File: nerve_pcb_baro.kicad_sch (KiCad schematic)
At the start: 5 parts

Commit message: Update schematics
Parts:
- JP2: footprint (none) -> Jumper:SolderJumper-2_P1.3mm_Open_TrianglePad1.0x1.5mm
- R22: renamed from R21; footprint (none) -> Resistor_SMD:R_0402_1005Metric
- R23: renamed from R22; footprint (none) -> Resistor_SMD:R_0402_1005Metric
- R24: renamed from R23; footprint (none) -> Resistor_SMD:R_0402_1005Metric
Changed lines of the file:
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@@
 			)
 		)
-		(property "Footprint" ""
+		(property "Footprint" "Jumper:SolderJumper-2_P1.3mm_Open_TrianglePad1.0x1.5mm"
 			(at 185.42 106.68 0)
 			(effects
@@
 		(dnp no)
 		(fields_autoplaced yes)
-		(property "Reference" "#PWR063"
+		(property "Reference" "#PWR062"
 			(at 137.16 115.57 0)
 			(effects
@@
 			(project "nerve_pcb"
 				(path "/c0277862-b3f2-4e0e-986f-34702f0543f0/9de129d2-0f7b-4a2d-85ad-214e335f6288"
-					(reference "#PWR063")
+					(reference "#PWR062")
 					(unit 1)
 				)
@@
 		(on_board yes)
 		(dnp no)
-		(property "Reference" "#PWR059"
+		(property "Reference" "#PWR058"
 			(at 177.8 95.25 0)
 			(effects
@@
 			(project "nerve_pcb"
 				(path "/c0277862-b3f2-4e0e-986f-34702f0543f0/9de129d2-0f7b-4a2d-85ad-214e335f6288"
-					(reference "#PWR059")
+					(reference "#PWR058")
 					(unit 1)
 				)
@@
 		(on_board yes)
 		(dnp no)
-		(property "Reference" "R22"
+		(property "Reference" "R23"
 			(at 180.34 95.2499 0)
 			(effects
@@
 			)
 		)
-		(property "Footprint" ""
+		(property "Footprint" "Resistor_SMD:R_0402_1005Metric"
 			(at 176.022 96.52 90)
 			(effects
@@
 			(project "nerve_pcb"
 				(path "/c0277862-b3f2-4e0e-986f-34702f0543f0/9de129d2-0f7b-4a2d-85ad-214e335f6288"
-					(reference "R22")
+					(reference "R23")
 					(unit 1)
 				)
@@
 		(on_board yes)
 		(dnp no)
-		(property "Reference" "#PWR058"
+		(property "Reference" "#PWR057"
 			(at 156.21 92.71 0)
 			(effects
@@
 			(project "nerve_pcb"
 				(path "/c0277862-b3f2-4e0e-986f-34702f0543f0/9de129d2-0f7b-4a2d-85ad-214e335f6288"
-					(reference "#PWR058")
+					(reference "#PWR057")
 					(unit 1)
 				)
@@
 		(on_board yes)
 		(dnp no)
-		(property "Reference" "R21"
+		(property "Reference" "R22"
 			(at 158.75 92.7099 0)
 			(effects
@@
 			)
 		)
-		(property "Footprint" ""
+		(property "Footprint" "Resistor_SMD:R_0402_1005Metric"
 			(at 154.432 93.98 90)
 			(effects
@@
 			(project "nerve_pcb"
 				(path "/c0277862-b3f2-4e0e-986f-34702f0543f0/9de129d2-0f7b-4a2d-85ad-214e335f6288"
-					(reference "R21")
+					(reference "R22")
 					(unit 1)
 				)
@@
 		(on_board yes)
 		(dnp no)
-		(property "Reference" "R23"
+		(property "Reference" "R24"
 			(at 111.76 100.3299 0)
 			(effects
@@
 			)
 		)
-		(property "Footprint" ""
+		(property "Footprint" "Resistor_SMD:R_0402_1005Metric"
 			(at 116.078 101.6 90)
 			(effects
@@
 			(project "nerve_pcb"
 				(path "/c0277862-b3f2-4e0e-986f-34702f0543f0/9de129d2-0f7b-4a2d-85ad-214e335f6288"
-					(reference "R23")
+					(reference "R24")
 					(unit 1)
 				)
@@
 		(dnp no)
 		(fields_autoplaced yes)
-		(property "Reference" "#PWR062"
+		(property "Reference" "#PWR061"
 			(at 190.5 114.3 0)
 			(effects
@@
 			(project "nerve_pcb"
 				(path "/c0277862-b3f2-4e0e-986f-34702f0543f0/9de129d2-0f7b-4a2d-85ad-214e335f6288"
-					(reference "#PWR062")
+					(reference "#PWR061")
 					(unit 1)
 				)
@@
 		(on_board yes)
 		(dnp no)
-		(property "Reference" "#PWR057"
+		(property "Reference" "#PWR056"
 			(at 139.7 87.63 0)
 			(effects
@@
 			(project "nerve_pcb"
 				(path "/c0277862-b3f2-4e0e-986f-34702f0543f0/9de129d2-0f7b-4a2d-85ad-214e335f6288"
-					(reference "#PWR057")
+					(reference "#PWR056")
 					(unit 1)
 				)
@@
 		(on_board yes)
 		(dnp no)
-		(property "Reference" "#PWR060"
+		(property "Reference" "#PWR059"
 			(at 123.19 96.52 0)
 			(effects
@@
 			(project "nerve_pcb"
 				(path "/c0277862-b3f2-4e0e-986f-34702f0543f0/9de129d2-0f7b-4a2d-85ad-214e335f6288"
-					(reference "#PWR060")
+					(reference "#PWR059")
 					(unit 1)
 				)
@@
 		(on_board yes)
 		(dnp no)
-		(property "Reference" "#PWR061"
+		(property "Reference" "#PWR060"
 			(at 114.3 100.33 0)
 			(effects
@@
 			(project "nerve_pcb"
 				(path "/c0277862-b3f2-4e0e-986f-34702f0543f0/9de129d2-0f7b-4a2d-85ad-214e335f6288"
-					(reference "#PWR061")
-					(unit 1)
-				)
+					(reference "#PWR060")
+					(unit 1)
+				)

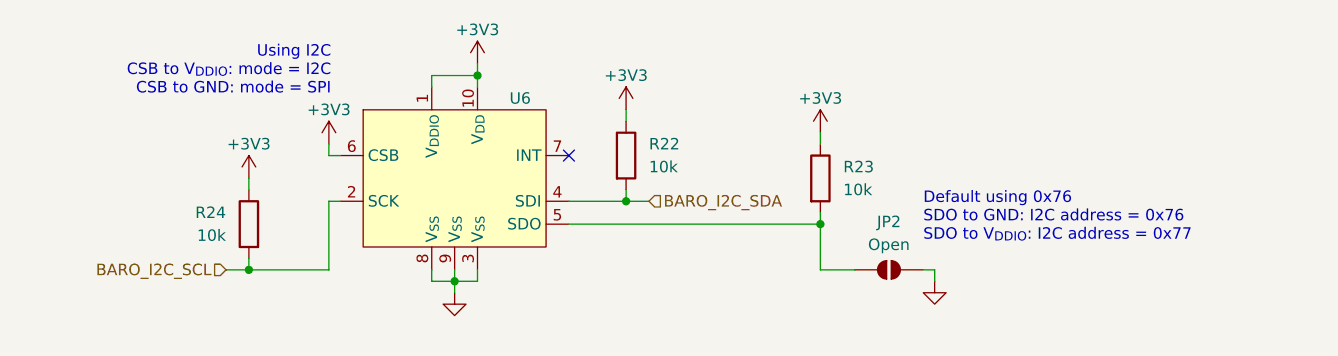
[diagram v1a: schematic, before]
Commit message: Add schematic changes from PCB routing/layout
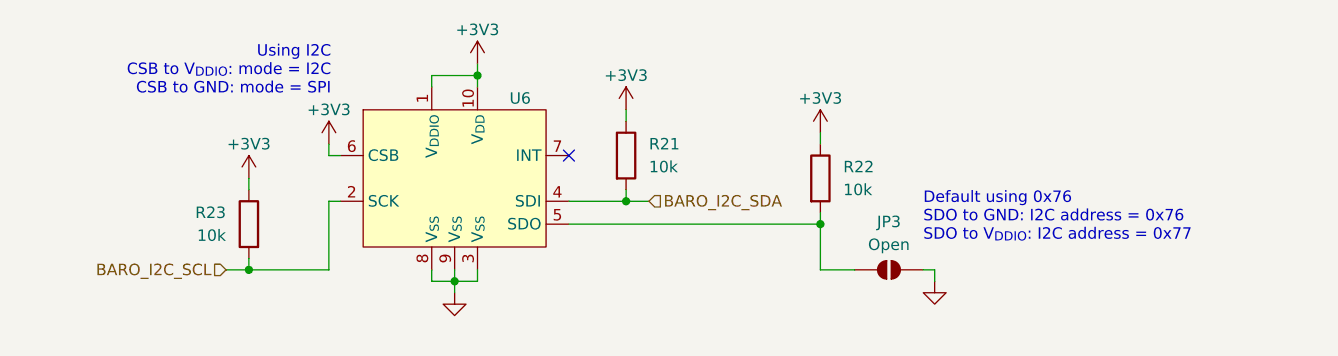
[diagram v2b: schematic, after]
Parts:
- renumbered JP2 to JP3, R22 to R21, R23 to R22, R24 to R23
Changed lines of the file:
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@@
 		(on_board yes)
 		(dnp no)
-		(property "Reference" "JP2"
+		(property "Reference" "JP3"
 			(at 185.42 101.346 0)
 			(effects
@@
 			(project ""
 				(path "/c0277862-b3f2-4e0e-986f-34702f0543f0/9de129d2-0f7b-4a2d-85ad-214e335f6288"
-					(reference "JP2")
+					(reference "JP3")
 					(unit 1)
 				)
@@
 		(dnp no)
 		(fields_autoplaced yes)
-		(property "Reference" "#PWR062"
+		(property "Reference" "#PWR060"
 			(at 137.16 115.57 0)
 			(effects
@@
 			(project "nerve_pcb"
 				(path "/c0277862-b3f2-4e0e-986f-34702f0543f0/9de129d2-0f7b-4a2d-85ad-214e335f6288"
-					(reference "#PWR062")
+					(reference "#PWR060")
 					(unit 1)
 				)
@@
 		(on_board yes)
 		(dnp no)
-		(property "Reference" "#PWR058"
+		(property "Reference" "#PWR056"
 			(at 177.8 95.25 0)
 			(effects
@@
 			(project "nerve_pcb"
 				(path "/c0277862-b3f2-4e0e-986f-34702f0543f0/9de129d2-0f7b-4a2d-85ad-214e335f6288"
-					(reference "#PWR058")
+					(reference "#PWR056")
 					(unit 1)
 				)
@@
 		(on_board yes)
 		(dnp no)
-		(property "Reference" "R23"
+		(property "Reference" "R22"
 			(at 180.34 95.2499 0)
 			(effects
@@
 			(project "nerve_pcb"
 				(path "/c0277862-b3f2-4e0e-986f-34702f0543f0/9de129d2-0f7b-4a2d-85ad-214e335f6288"
-					(reference "R23")
+					(reference "R22")
 					(unit 1)
 				)
@@
 		(on_board yes)
 		(dnp no)
-		(property "Reference" "#PWR057"
+		(property "Reference" "#PWR055"
 			(at 156.21 92.71 0)
 			(effects
@@
 			(project "nerve_pcb"
 				(path "/c0277862-b3f2-4e0e-986f-34702f0543f0/9de129d2-0f7b-4a2d-85ad-214e335f6288"
-					(reference "#PWR057")
+					(reference "#PWR055")
 					(unit 1)
 				)
@@
 		(on_board yes)
 		(dnp no)
-		(property "Reference" "R22"
+		(property "Reference" "R21"
 			(at 158.75 92.7099 0)
 			(effects
@@
 			(project "nerve_pcb"
 				(path "/c0277862-b3f2-4e0e-986f-34702f0543f0/9de129d2-0f7b-4a2d-85ad-214e335f6288"
-					(reference "R22")
+					(reference "R21")
 					(unit 1)
 				)
@@
 		(on_board yes)
 		(dnp no)
-		(property "Reference" "R24"
+		(property "Reference" "R23"
 			(at 111.76 100.3299 0)
 			(effects
@@
 			(project "nerve_pcb"
 				(path "/c0277862-b3f2-4e0e-986f-34702f0543f0/9de129d2-0f7b-4a2d-85ad-214e335f6288"
-					(reference "R24")
+					(reference "R23")
 					(unit 1)
 				)
@@
 		(dnp no)
 		(fields_autoplaced yes)
-		(property "Reference" "#PWR061"
+		(property "Reference" "#PWR059"
 			(at 190.5 114.3 0)
 			(effects
@@
 			(project "nerve_pcb"
 				(path "/c0277862-b3f2-4e0e-986f-34702f0543f0/9de129d2-0f7b-4a2d-85ad-214e335f6288"
-					(reference "#PWR061")
+					(reference "#PWR059")
 					(unit 1)
 				)
@@
 		(on_board yes)
 		(dnp no)
-		(property "Reference" "#PWR056"
+		(property "Reference" "#PWR054"
 			(at 139.7 87.63 0)
 			(effects
@@
 			(project "nerve_pcb"
 				(path "/c0277862-b3f2-4e0e-986f-34702f0543f0/9de129d2-0f7b-4a2d-85ad-214e335f6288"
-					(reference "#PWR056")
+					(reference "#PWR054")
 					(unit 1)
 				)
@@
 		(on_board yes)
 		(dnp no)
-		(property "Reference" "#PWR059"
+		(property "Reference" "#PWR057"
 			(at 123.19 96.52 0)
 			(effects
@@
 			(project "nerve_pcb"
 				(path "/c0277862-b3f2-4e0e-986f-34702f0543f0/9de129d2-0f7b-4a2d-85ad-214e335f6288"
-					(reference "#PWR059")
+					(reference "#PWR057")
 					(unit 1)
 				)
@@
 		(on_board yes)
 		(dnp no)
-		(property "Reference" "#PWR060"
+		(property "Reference" "#PWR058"
 			(at 114.3 100.33 0)
 			(effects
@@
 			(project "nerve_pcb"
 				(path "/c0277862-b3f2-4e0e-986f-34702f0543f0/9de129d2-0f7b-4a2d-85ad-214e335f6288"
-					(reference "#PWR060")
-					(unit 1)
-				)
+					(reference "#PWR058")
+					(unit 1)
+				)

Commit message: Update refs on schematics
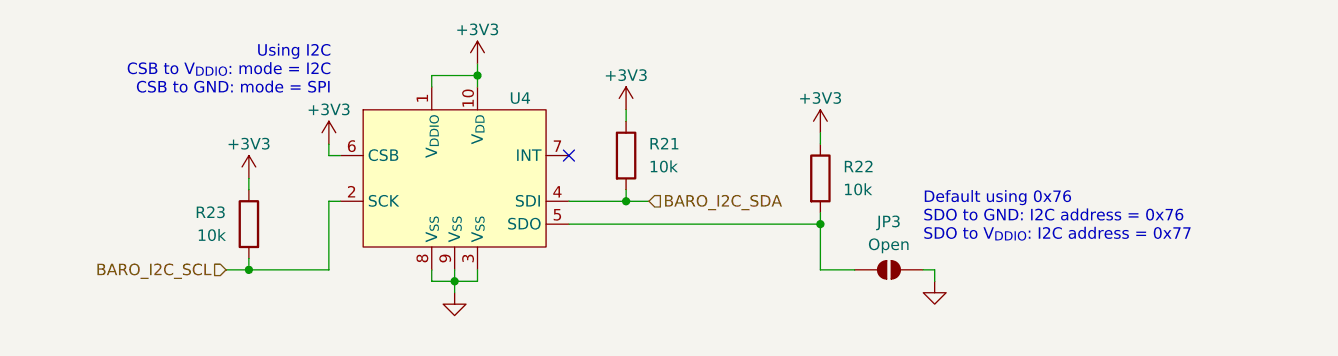
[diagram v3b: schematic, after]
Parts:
- renumbered U6 to U4
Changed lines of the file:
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@@
 		(dnp no)
 		(fields_autoplaced yes)
-		(property "Reference" "#PWR060"
+		(property "Reference" "#PWR076"
 			(at 137.16 115.57 0)
 			(effects
@@
 			(project "nerve_pcb"
 				(path "/c0277862-b3f2-4e0e-986f-34702f0543f0/9de129d2-0f7b-4a2d-85ad-214e335f6288"
-					(reference "#PWR060")
+					(reference "#PWR076")
 					(unit 1)
 				)
@@
 		(on_board yes)
 		(dnp no)
-		(property "Reference" "#PWR056"
+		(property "Reference" "#PWR072"
 			(at 177.8 95.25 0)
 			(effects
@@
 			(project "nerve_pcb"
 				(path "/c0277862-b3f2-4e0e-986f-34702f0543f0/9de129d2-0f7b-4a2d-85ad-214e335f6288"
-					(reference "#PWR056")
+					(reference "#PWR072")
 					(unit 1)
 				)
@@
 		(on_board yes)
 		(dnp no)
-		(property "Reference" "#PWR055"
+		(property "Reference" "#PWR071"
 			(at 156.21 92.71 0)
 			(effects
@@
 			(project "nerve_pcb"
 				(path "/c0277862-b3f2-4e0e-986f-34702f0543f0/9de129d2-0f7b-4a2d-85ad-214e335f6288"
-					(reference "#PWR055")
+					(reference "#PWR071")
 					(unit 1)
 				)
@@
 		(on_board yes)
 		(dnp no)
-		(property "Reference" "U6"
+		(property "Reference" "U4"
 			(at 143.256 87.63 0)
 			(effects
@@
 			(project ""
 				(path "/c0277862-b3f2-4e0e-986f-34702f0543f0/9de129d2-0f7b-4a2d-85ad-214e335f6288"
-					(reference "U6")
+					(reference "U4")
 					(unit 1)
 				)
@@
 		(dnp no)
 		(fields_autoplaced yes)
-		(property "Reference" "#PWR059"
+		(property "Reference" "#PWR075"
 			(at 190.5 114.3 0)
 			(effects
@@
 			(project "nerve_pcb"
 				(path "/c0277862-b3f2-4e0e-986f-34702f0543f0/9de129d2-0f7b-4a2d-85ad-214e335f6288"
-					(reference "#PWR059")
+					(reference "#PWR075")
 					(unit 1)
 				)
@@
 		(on_board yes)
 		(dnp no)
-		(property "Reference" "#PWR054"
+		(property "Reference" "#PWR070"
 			(at 139.7 87.63 0)
 			(effects
@@
 			(project "nerve_pcb"
 				(path "/c0277862-b3f2-4e0e-986f-34702f0543f0/9de129d2-0f7b-4a2d-85ad-214e335f6288"
-					(reference "#PWR054")
+					(reference "#PWR070")
 					(unit 1)
 				)
@@
 		(on_board yes)
 		(dnp no)
-		(property "Reference" "#PWR057"
+		(property "Reference" "#PWR073"
 			(at 123.19 96.52 0)
 			(effects
@@
 			(project "nerve_pcb"
 				(path "/c0277862-b3f2-4e0e-986f-34702f0543f0/9de129d2-0f7b-4a2d-85ad-214e335f6288"
-					(reference "#PWR057")
+					(reference "#PWR073")
 					(unit 1)
 				)
@@
 		(on_board yes)
 		(dnp no)
-		(property "Reference" "#PWR058"
+		(property "Reference" "#PWR074"
 			(at 114.3 100.33 0)
 			(effects
@@
 			(project "nerve_pcb"
 				(path "/c0277862-b3f2-4e0e-986f-34702f0543f0/9de129d2-0f7b-4a2d-85ad-214e335f6288"
-					(reference "#PWR058")
-					(unit 1)
-				)
+					(reference "#PWR074")
+					(unit 1)
+				)

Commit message: Revert to 603 package sizes and add WIP PCB
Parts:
- R21, R22, R23: footprint Resistor_SMD:R_0402_1005Metric -> Resistor_SMD:R_0603_1608Metric
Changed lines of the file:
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@@
 			)
 		)
-		(property "Footprint" "Resistor_SMD:R_0402_1005Metric"
+		(property "Footprint" "Resistor_SMD:R_0603_1608Metric"
 			(at 176.022 96.52 90)
 			(effects
@@
 			)
 		)
-		(property "Footprint" "Resistor_SMD:R_0402_1005Metric"
+		(property "Footprint" "Resistor_SMD:R_0603_1608Metric"
 			(at 154.432 93.98 90)
 			(effects
@@
 			)
 		)
-		(property "Footprint" "Resistor_SMD:R_0402_1005Metric"
+		(property "Footprint" "Resistor_SMD:R_0603_1608Metric"
 			(at 116.078 101.6 90)
 			(effects

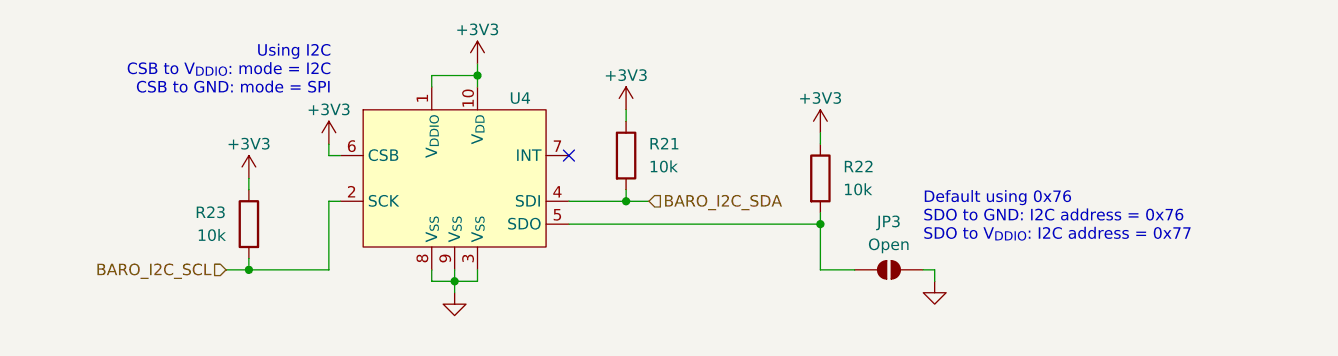
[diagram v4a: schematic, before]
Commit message: Split and remove add-on board designs
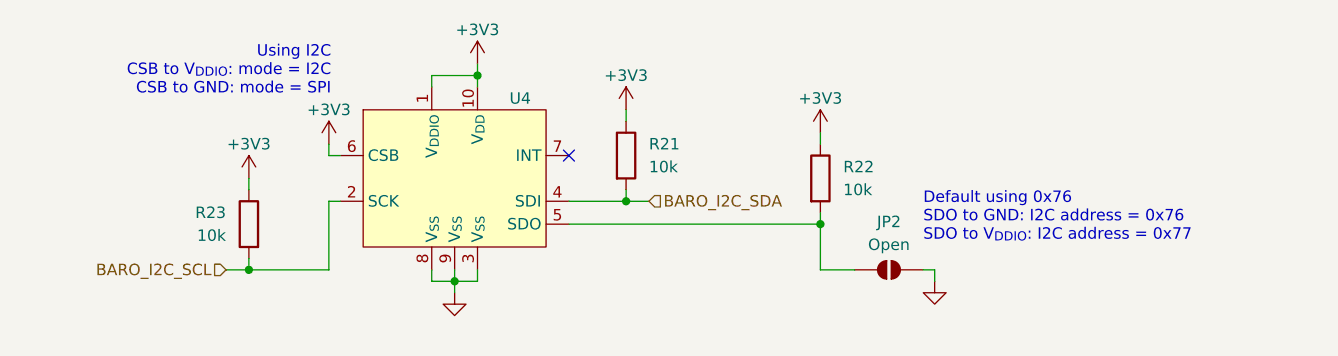
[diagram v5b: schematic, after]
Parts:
- renumbered JP3 to JP2
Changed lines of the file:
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@@
 		(on_board yes)
 		(dnp no)
-		(property "Reference" "JP3"
+		(property "Reference" "JP2"
 			(at 185.42 101.346 0)
 			(effects
@@
 			(project ""
 				(path "/c0277862-b3f2-4e0e-986f-34702f0543f0/9de129d2-0f7b-4a2d-85ad-214e335f6288"
-					(reference "JP3")
+					(reference "JP2")
 					(unit 1)
 				)
@@
 		(dnp no)
 		(fields_autoplaced yes)
-		(property "Reference" "#PWR076"
+		(property "Reference" "#PWR075"
 			(at 137.16 115.57 0)
 			(effects
@@
 			(project "nerve_pcb"
 				(path "/c0277862-b3f2-4e0e-986f-34702f0543f0/9de129d2-0f7b-4a2d-85ad-214e335f6288"
-					(reference "#PWR076")
+					(reference "#PWR075")
 					(unit 1)
 				)
@@
 		(on_board yes)
 		(dnp no)
-		(property "Reference" "#PWR072"
+		(property "Reference" "#PWR071"
 			(at 177.8 95.25 0)
 			(effects
@@
 			(project "nerve_pcb"
 				(path "/c0277862-b3f2-4e0e-986f-34702f0543f0/9de129d2-0f7b-4a2d-85ad-214e335f6288"
-					(reference "#PWR072")
+					(reference "#PWR071")
 					(unit 1)
 				)
@@
 		(on_board yes)
 		(dnp no)
-		(property "Reference" "#PWR071"
+		(property "Reference" "#PWR070"
 			(at 156.21 92.71 0)
 			(effects
@@
 			(project "nerve_pcb"
 				(path "/c0277862-b3f2-4e0e-986f-34702f0543f0/9de129d2-0f7b-4a2d-85ad-214e335f6288"
-					(reference "#PWR071")
+					(reference "#PWR070")
 					(unit 1)
 				)
@@
 		(dnp no)
 		(fields_autoplaced yes)
-		(property "Reference" "#PWR075"
+		(property "Reference" "#PWR074"
 			(at 190.5 114.3 0)
 			(effects
@@
 			(project "nerve_pcb"
 				(path "/c0277862-b3f2-4e0e-986f-34702f0543f0/9de129d2-0f7b-4a2d-85ad-214e335f6288"
-					(reference "#PWR075")
+					(reference "#PWR074")
 					(unit 1)
 				)
@@
 		(on_board yes)
 		(dnp no)
-		(property "Reference" "#PWR070"
+		(property "Reference" "#PWR069"
 			(at 139.7 87.63 0)
 			(effects
@@
 			(project "nerve_pcb"
 				(path "/c0277862-b3f2-4e0e-986f-34702f0543f0/9de129d2-0f7b-4a2d-85ad-214e335f6288"
-					(reference "#PWR070")
+					(reference "#PWR069")
 					(unit 1)
 				)
@@
 		(on_board yes)
 		(dnp no)
-		(property "Reference" "#PWR073"
+		(property "Reference" "#PWR072"
 			(at 123.19 96.52 0)
 			(effects
@@
 			(project "nerve_pcb"
 				(path "/c0277862-b3f2-4e0e-986f-34702f0543f0/9de129d2-0f7b-4a2d-85ad-214e335f6288"
-					(reference "#PWR073")
+					(reference "#PWR072")
 					(unit 1)
 				)
@@
 		(on_board yes)
 		(dnp no)
-		(property "Reference" "#PWR074"
+		(property "Reference" "#PWR073"
 			(at 114.3 100.33 0)
 			(effects
@@
 			(project "nerve_pcb"
 				(path "/c0277862-b3f2-4e0e-986f-34702f0543f0/9de129d2-0f7b-4a2d-85ad-214e335f6288"
-					(reference "#PWR074")
-					(unit 1)
-				)
+					(reference "#PWR073")
+					(unit 1)
+				)

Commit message: Clean up schematics and ensure PCB parity
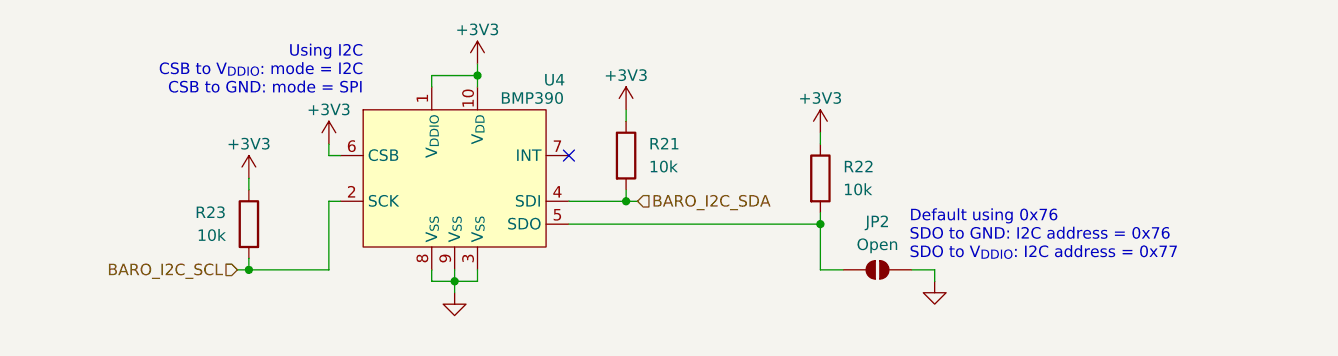
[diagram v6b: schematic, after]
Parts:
- U4: value ~ -> BMP390
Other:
- moved on the sheet: JP2
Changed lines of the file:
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@@
 	(wire
 		(pts
-			(xy 111.76 106.68) (xy 114.3 106.68)
+			(xy 113.03 106.68) (xy 114.3 106.68)
 		)
 		(stroke
@@
 	(wire
 		(pts
-			(xy 189.23 106.68) (xy 190.5 106.68)
+			(xy 187.96 106.68) (xy 190.5 106.68)
 		)
 		(stroke
@@
 	(wire
 		(pts
-			(xy 158.75 99.06) (xy 156.21 99.06)
+			(xy 157.48 99.06) (xy 156.21 99.06)
 		)
 		(stroke
@@
 	(wire
 		(pts
-			(xy 177.8 106.68) (xy 181.61 106.68)
+			(xy 177.8 106.68) (xy 180.34 106.68)
 		)
 		(stroke
@@
 	(text "Default using 0x76\nSDO to GND: I2C address = 0x76\nSDO to V_{DDIO}: I2C address = 0x77"
 		(exclude_from_sim no)
-		(at 189.23 100.838 0)
+		(at 187.706 102.87 0)
 		(effects
 			(font
@@
 	(text "Using I2C\nCSB to V_{DDIO}: mode = I2C\nCSB to GND: mode = SPI"
 		(exclude_from_sim no)
-		(at 123.444 84.582 0)
+		(at 127 84.582 0)
 		(effects
 			(font
@@
 	(hierarchical_label "BARO_I2C_SDA"
 		(shape input)
-		(at 158.75 99.06 0)
+		(at 157.48 99.06 0)
 		(fields_autoplaced yes)
 		(effects
@@
 	(hierarchical_label "BARO_I2C_SCL"
 		(shape input)
-		(at 111.76 106.68 180)
+		(at 113.03 106.68 180)
 		(fields_autoplaced yes)
 		(effects
@@
 	(symbol
 		(lib_id "Jumper:SolderJumper_2_Open")
-		(at 185.42 106.68 0)
+		(at 184.15 106.68 0)
 		(unit 1)
 		(exclude_from_sim yes)
@@
 		(dnp no)
 		(property "Reference" "JP2"
-			(at 185.42 101.346 0)
+			(at 184.15 101.346 0)
 			(effects
 				(font
@@
 		)
 		(property "Value" "Open"
-			(at 185.42 103.886 0)
+			(at 184.15 103.886 0)
 			(effects
 				(font
@@
 		)
 		(property "Footprint" "Jumper:SolderJumper-2_P1.3mm_Open_TrianglePad1.0x1.5mm"
-			(at 185.42 106.68 0)
+			(at 184.15 106.68 0)
 			(effects
 				(font
@@
 		)
 		(property "Datasheet" "~"
-			(at 185.42 106.68 0)
+			(at 184.15 106.68 0)
 			(effects
 				(font
@@
 		)
 		(property "Description" "Solder Jumper, 2-pole, open"
-			(at 185.42 106.68 0)
+			(at 184.15 106.68 0)
 			(effects
 				(font
@@
 		(dnp no)
 		(property "Reference" "U4"
-			(at 143.256 87.63 0)
+			(at 147.066 85.598 0)
 			(effects
 				(font
@@
 			)
 		)
-		(property "Value" "~"
-			(at 141.8941 87.63 0)
-			(effects
-				(font
+		(property "Value" "BMP390"
+			(at 142.24 87.63 0)
+			(effects
+				(font
